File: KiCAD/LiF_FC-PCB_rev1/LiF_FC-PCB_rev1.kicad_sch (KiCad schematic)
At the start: 0 parts

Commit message: progress backup before increasing the size of the PCB again
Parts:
- added H1, H2, H3: MountingHole, MountingHole:MountingHole_3.2mm_M3_DIN965, symbol Mechanical:MountingHole
- added J45: Conn_01x10_Socket, Connector_PinHeader_2.54mm:PinHeader_1x10_P2.54mm_Vertical, symbol Connector:Conn_01x10_Socket
- added J46: Conn_01x22_Socket, Connector_PinHeader_2.54mm:PinHeader_1x22_P2.54mm_Vertical, symbol Connector:Conn_01x22_Socket
- added J47: Conn_01x16_Pin, Connector_PinHeader_2.54mm:PinHeader_1x16_P2.54mm_Vertical, symbol Connector:Conn_01x16_Pin

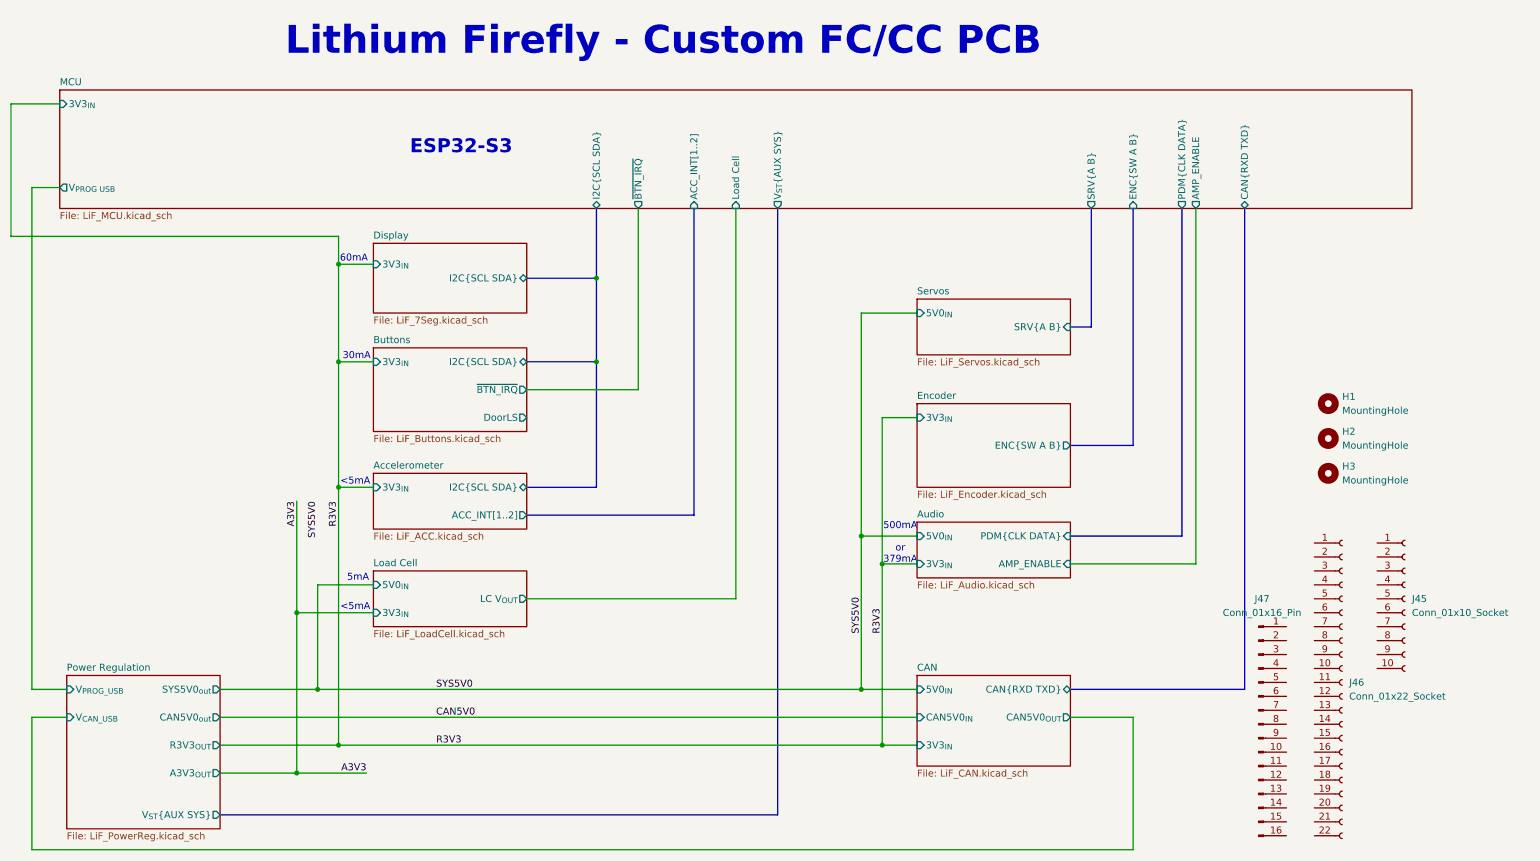
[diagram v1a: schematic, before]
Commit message: Created new KiCAD project for IO PCB, moved relevant components there, saving backup before reannotating the Service PCB schematics
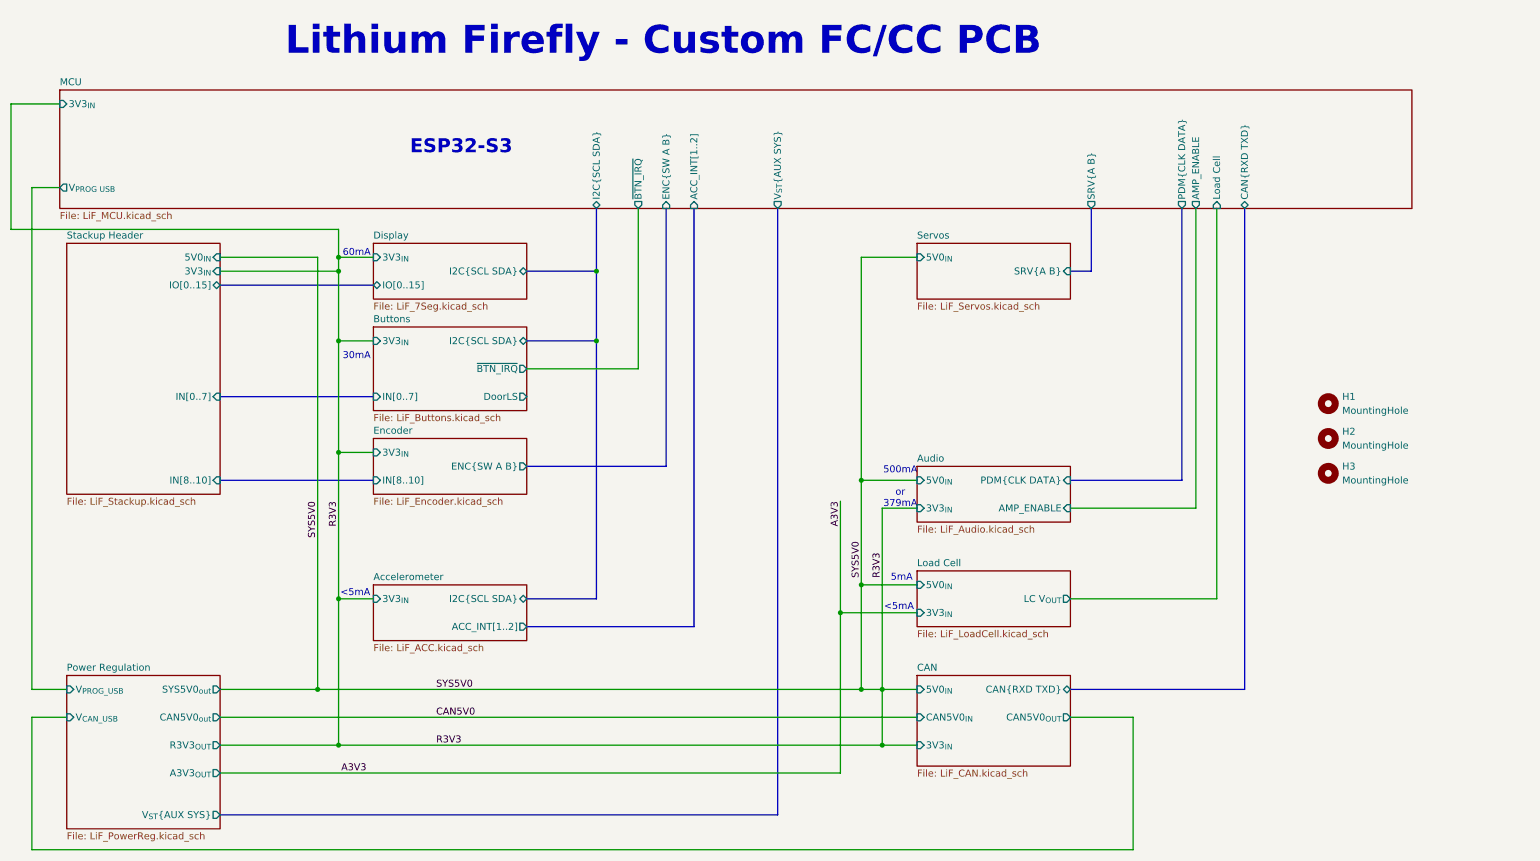
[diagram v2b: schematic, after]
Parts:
- removed J45: Conn_01x10_Socket, Connector_PinHeader_2.54mm:PinHeader_1x10_P2.54mm_Vertical, symbol Connector:Conn_01x10_Socket
- removed J46: Conn_01x22_Socket, Connector_PinHeader_2.54mm:PinHeader_1x22_P2.54mm_Vertical, symbol Connector:Conn_01x22_Socket
- removed J47: Conn_01x16_Pin, Connector_PinHeader_2.54mm:PinHeader_1x16_P2.54mm_Vertical, symbol Connector:Conn_01x16_Pin
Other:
- added sheet Stackup Header (LiF_Stackup.kicad_sch)
- sheet Buttons ports: added IN[0..7]; removed none
- sheet Display ports: added IO[0..15]; removed none
- sheet Encoder ports: added IN[8..10]; removed none

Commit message: backup before redoing the analog section
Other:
- sheet Encoder ports: added none; removed 3V3_{IN}

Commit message: progress save for the night. landmarking of service PCB is almost done. redid the analog section layout to make it more assembleable and better utilze the space. Still need to do ACC, R3V3, IO, test points, and jumpers
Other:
- sheet Buttons ports: added IO[16..23]; removed none
- sheet Load Cell ports: added IA_EN; removed none
- sheet MCU ports: added DoorLS, IA_EN; removed none
- sheet Stackup Header ports: added IO[16..23]; removed none
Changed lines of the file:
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@@
 	(text "500mA\n\nor\n379mA"
 		(exclude_from_sim no)
-		(at 177.292 99.06 0)
+		(at 177.292 92.71 0)
 		(effects
 			(font
@@
 	(text "5mA"
 		(exclude_from_sim no)
-		(at 177.546 115.57 0)
+		(at 177.546 108.458 0)
 		(effects
 			(font
@@
 	)
 	(junction
+		(at 170.18 91.44)
+		(diameter 0)
+		(color 0 0 0 0)
+	)
+	(junction
 		(at 166.37 121.92)
 		(diameter 0)
@@
 	)
 	(junction
-		(at 170.18 97.79)
+		(at 170.18 109.22)
 		(diameter 0)
 		(color 0 0 0 0)
@@
 	)
 	(junction
-		(at 170.18 116.84)
-		(diameter 0)
-		(color 0 0 0 0)
-	)
-	(junction
 		(at 74.93 57.15)
 		(diameter 0)
@@
 	(wire
 		(pts
-			(xy 234.95 119.38) (xy 208.28 119.38)
+			(xy 234.95 114.3) (xy 208.28 114.3)
 		)
 		(stroke
@@
 	(wire
 		(pts
-			(xy 173.99 102.87) (xy 173.99 146.05)
+			(xy 173.99 96.52) (xy 173.99 146.05)
 		)
 		(stroke
@@
 	(wire
 		(pts
-			(xy 170.18 116.84) (xy 180.34 116.84)
+			(xy 170.18 109.22) (xy 180.34 109.22)
 		)
 		(stroke
@@
 	(wire
 		(pts
-			(xy 170.18 97.79) (xy 170.18 116.84)
+			(xy 170.18 109.22) (xy 170.18 135.89)
+		)
+		(stroke
+			(width 0)
+			(type default)
+		)
+	)
+	(wire
+		(pts
+			(xy 237.49 48.26) (xy 237.49 118.11)
+		)
+		(stroke
+			(width 0)
+			(type default)
+		)
+	)
+	(wire
+		(pts
+			(xy 132.08 48.26) (xy 132.08 82.55)
+		)
+		(stroke
+			(width 0)
+			(type default)
+		)
+	)
+	(wire
+		(pts
+			(xy 170.18 91.44) (xy 170.18 109.22)
 		)
 		(stroke
@@
 	(wire
 		(pts
-			(xy 170.18 57.15) (xy 170.18 97.79)
+			(xy 170.18 57.15) (xy 170.18 91.44)
 		)
 		(stroke
@@
 	(wire
 		(pts
-			(xy 231.14 48.26) (xy 231.14 102.87)
+			(xy 231.14 48.26) (xy 231.14 96.52)
 		)
 		(stroke
@@
 		)
 	)
+	(wire
+		(pts
+			(xy 132.08 82.55) (xy 109.22 82.55)
+		)
+		(stroke
+			(width 0)
+			(type default)
+		)
+	)
 	(bus
 		(pts
-			(xy 240.03 48.26) (xy 240.03 135.89)
+			(xy 245.11 48.26) (xy 245.11 135.89)
 		)
 		(stroke
@@
 	(wire
 		(pts
-			(xy 234.95 48.26) (xy 234.95 119.38)
+			(xy 234.95 48.26) (xy 234.95 114.3)
 		)
 		(stroke
@@
 	(bus
 		(pts
-			(xy 240.03 135.89) (xy 208.28 135.89)
+			(xy 245.11 135.89) (xy 208.28 135.89)
 		)
 		(stroke
@@
 		)
 	)
-	(wire
-		(pts
-			(xy 170.18 116.84) (xy 170.18 135.89)
-		)
-		(stroke
-			(width 0)
-			(type default)
-		)
-	)
 	(bus
 		(pts
@@
 	(wire
 		(pts
-			(xy 180.34 102.87) (xy 173.99 102.87)
+			(xy 180.34 96.52) (xy 173.99 96.52)
 		)
 		(stroke
@@
 	(bus
 		(pts
-			(xy 208.28 97.79) (xy 228.6 97.79)
+			(xy 208.28 91.44) (xy 228.6 91.44)
 		)
 		(stroke
@@
 	(wire
 		(pts
-			(xy 208.28 102.87) (xy 231.14 102.87)
+			(xy 208.28 96.52) (xy 231.14 96.52)
 		)
 		(stroke
@@
 	(wire
 		(pts
-			(xy 170.18 97.79) (xy 180.34 97.79)
+			(xy 170.18 91.44) (xy 180.34 91.44)
+		)
+		(stroke
+			(width 0)
+			(type default)
+		)
+	)
+	(bus
+		(pts
+			(xy 53.34 80.01) (xy 81.28 80.01)
+		)
+		(stroke
+			(width 0)
+			(type default)
+		)
+	)
+	(wire
+		(pts
+			(xy 237.49 118.11) (xy 208.28 118.11)
 		)
 		(stroke
@@
 	(bus
 		(pts
-			(xy 228.6 48.26) (xy 228.6 97.79)
+			(xy 228.6 48.26) (xy 228.6 91.44)
 		)
 		(stroke
@@
 	)
 	(sheet
-		(at 180.34 114.3)
-		(size 27.94 10.16)
+		(at 180.34 106.68)
+		(size 27.94 17.78)
 		(exclude_from_sim no)
 		(in_bom yes)
@@
 		)
 		(property "Sheetname" "Load Cell"
-			(at 180.34 113.5884 0)
+			(at 180.34 105.9684 0)
 			(effects
 				(font
@@
 		)
 		(pin "5V0_{IN}" input
-			(at 180.34 116.84 180)
+			(at 180.34 109.22 180)
 			(effects
 				(font
@@
 		)
 		(pin "LC V_{OUT}" output
-			(at 208.28 119.38 0)
+			(at 208.28 114.3 0)
+			(effects
+				(font
+					(size 1.27 1.27)
+				)
+				(justify right)
+			)
+		)
+		(pin "IA_EN" input
+			(at 208.28 118.11 0)
 			(effects
 				(font
@@
 			)
 		)
+		(pin "IO[16..23]" bidirectional
+			(at 53.34 80.01 0)
+			(effects
+				(font
+					(size 1.27 1.27)
+				)
+				(justify right)
+			)
+		)
 		(instances
 			(project "LiF_FC-PCB_rev1"
@@
 			)
 		)
+		(pin "IO[16..23]" bidirectional
+			(at 81.28 80.01 180)
+			(effects
+				(font
+					(size 1.27 1.27)
+				)
+				(justify left)
+			)
+		)
 		(instances
 			(project "LiF_FC-PCB_rev1"
@@
 	)
 	(sheet
-		(at 180.34 95.25)
+		(at 180.34 88.9)
 		(size 27.94 10.16)
 		(exclude_from_sim no)
@@
 		)
 		(property "Sheetname" "Audio"
-			(at 180.34 94.5384 0)
+			(at 180.34 88.1884 0)
 			(effects
 				(font
@@
 		)
 		(property "Sheetfile" "LiF_Audio.kicad_sch"
-			(at 180.34 105.9946 0)
+			(at 180.34 99.6446 0)
 			(effects
 				(font
@@
 		)
 		(pin "3V3_{IN}" input
-			(at 180.34 102.87 180)
+			(at 180.34 96.52 180)
 			(effects
 				(font
@@
 		)
 		(pin "5V0_{IN}" input
-			(at 180.34 97.79 180)
+			(at 180.34 91.44 180)
 			(effects
 				(font
@@
 		)
 		(pin "AMP_ENABLE" input
-			(at 208.28 102.87 0)
+			(at 208.28 96.52 0)
 			(effects
 				(font
@@
 		)
 		(pin "PDM{CLK DATA}" input
-			(at 208.28 97.79 0)
+			(at 208.28 91.44 0)
 			(effects
 				(font
@@
 		)
 		(pin "CAN{RXD TXD}" bidirectional
-			(at 240.03 48.26 270)
+			(at 245.11 48.26 270)
 			(effects
 				(font
@@
 			(effects
 				(font
+					(size 1.27 1.27)
+				)
+				(justify left)
+			)
+		)
+		(pin "DoorLS" input
+			(at 132.08 48.26 270)
+			(effects
+				(font
+					(size 1.27 1.27)
+				)
+				(justify left)
+			)
+		)
+		(pin "IA_EN" output
+			(at 237.49 48.26 270)
+			(effects
+				(font

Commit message: finished service PCB routing and silkscreen, finished IO PCB layout, routing, and silkscreen. Exported production files, submitted PCB for manufacturing by JLCPCB
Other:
- sheet Power Regulation ports: added V_{supply}; removed none
- sheet Stackup Header ports: added V_{supply}; removed none
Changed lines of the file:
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@@
+		)
+	)
+	(wire
+		(pts
+			(xy 21.59 97.79) (xy 25.4 97.79)
+		)
+		(stroke
+			(width 0)
+			(type default)
 		)
 	)
@@
 		)
 	)
+	(wire
+		(pts
+			(xy 21.59 158.75) (xy 21.59 97.79)
+		)
+		(stroke
+			(width 0)
+			(type default)
+		)
+	)
 	(bus
 		(pts
@@
 		(pts
 			(xy 121.92 59.69) (xy 121.92 48.26)
+		)
+		(stroke
+			(width 0)
+			(type default)
+		)
+	)
+	(wire
+		(pts
+			(xy 25.4 158.75) (xy 21.59 158.75)
 		)
 		(stroke
@@
 			)
 		)
+		(pin "V_{supply}" input
+			(at 25.4 97.79 180)
+			(effects
+				(font
+					(size 1.27 1.27)
+				)
+				(justify left)
+			)
+		)
 		(instances
 			(project "LiF_FC-PCB_rev1"
@@
 			)
 		)
+		(pin "V_{supply}" output
+			(at 25.4 158.75 180)
+			(effects
+				(font
+					(size 1.27 1.27)
+				)
+				(justify left)
+			)
+		)
